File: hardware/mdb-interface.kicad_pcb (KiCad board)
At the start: 2 copper layers, 99.6 x 99.1 mm, 80 parts, among them IC1 ATMEGA644PA-A, J1 USB, K1 *, K2 *, P1 CONN_24, P10 CONN_1, P11 CONN_1, P12 CONN_1, P2 CONN_12V, P3 CONN_6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

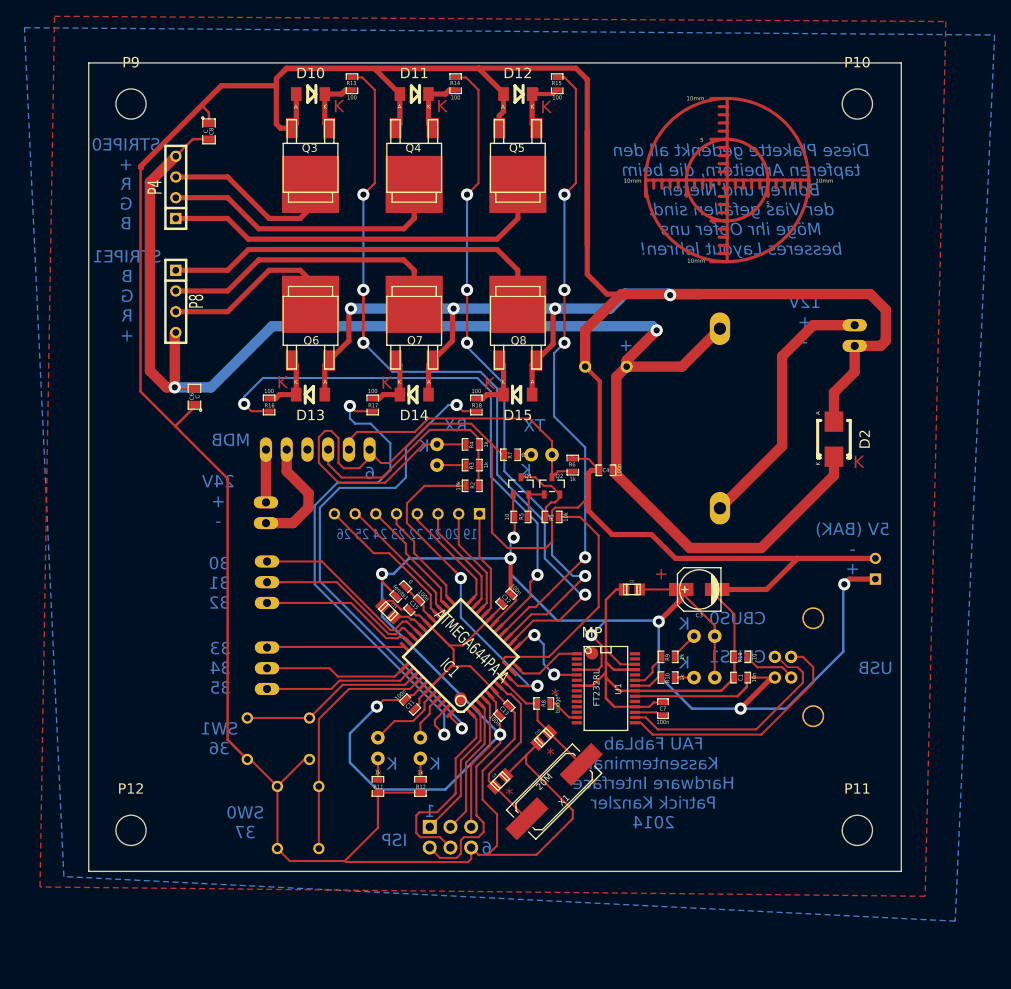
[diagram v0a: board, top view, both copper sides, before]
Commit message: Leiterplattenbemaßung gesäubert, fixes #14
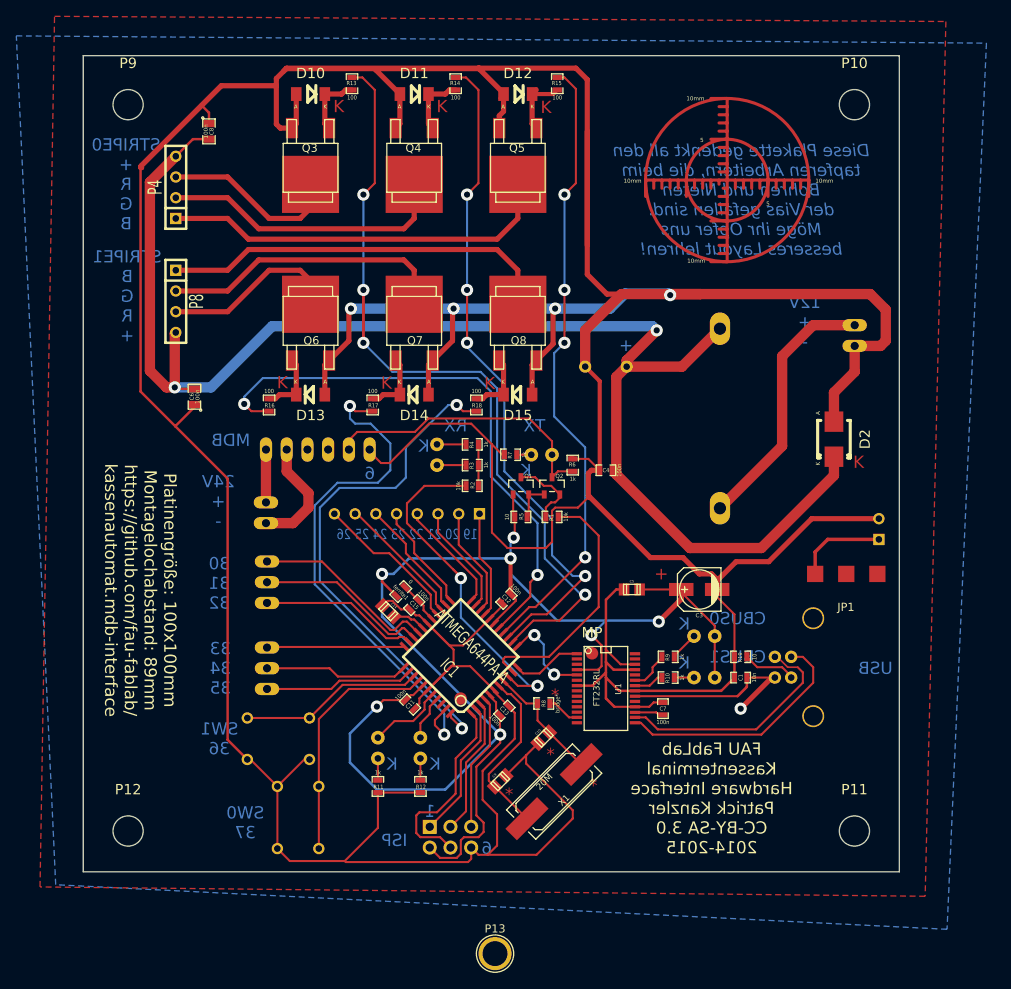
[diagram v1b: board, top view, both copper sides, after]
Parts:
- added JP1: JUMPER3, Oddities:NetTie-II_SMD, F.Cu at (163.4, 99.4)
- added P13: CONN_01X01, Connect:1pin, F.Cu at (120.4, 146.0)
- C6, C8: value C -> 100n
- moved P6 4.88 mm to (167.4, 93.9)
- moved P10 0.37 mm to (164.4, 41.9)
- moved P11 0.37 mm to (164.4, 130.9)
- moved P9 0.37 mm to (75.4, 41.9)
- moved P12 0.37 mm to (75.4, 130.9)
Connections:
- C1 pad 1: +5V -> /VUSB
- D1 pad 1: Net-(D1-Pad1) -> +5V
- D1 pad 2: GND -> Net-(D1-Pad2)
- J1 pad 1: +5V -> /VUSB
- P6 pad 1: +5V -> /VBAK
- R3 pad 1: /MDB_MR -> Net-(D1-Pad2)
- R3 pad 2: Net-(D1-Pad1) -> /MDB_MR
- R4 pad 1: /MDB_MR -> +5V
- R4 pad 2: GND -> /MDB_MR
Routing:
- net +5V: track 266.9 -> 206.2 mm, vias 9 -> 7
- net GND: track 875.1 -> 824.0 mm
- net /MDB_MR: track 30.4 -> 0.89 mm
- net /VUSB: track 0.00 -> 17.4 mm, vias 0 -> 1
- net /VBAK: track 0.00 -> 11.1 mm
- net Net-(D1-Pad2): track 0.00 -> 6.10 mm
- net Net-(D1-Pad1): track 3.56 -> 0.00 mm
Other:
- board size 99.6 x 99.1 mm -> 100 x 100 mm
- board text added: "FAU FabLab Kassenterminal Hardware Interface Patrick Kanzler CC-BY-SA 3.0 2014-2015"
- board text added: "Platinengröße: 100x100mm Montagelochabstand: 89mm https://github.com/fau-fablab/ kassenautomat.mdb-interface"
- board text removed: "FAU FabLab Kassenterminal Hardware Interface Patrick Kanzler 2014"

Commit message: Platine angepasst, bereit zur Fertigungsvorbereitung, fixes #11
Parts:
- removed MP (x2): Measurement_Point_Round-SMD-Pad_Small, Measurement_Points:Measurement_Point_Round-SMD-Pad_Small
- P13: footprint Connect:1pin -> Measurement_Points:Measurement_Point_Square-TH_Small
- moved P13 75.9 mm to (167.4, 86.4)
- moved Q2 1.17 mm to (128.5, 88.9), turned to 270 degrees
- moved Q1 1.02 mm to (124.1, 89.5), turned to 270 degrees
- turned D1 to 270 degrees
- turned R3 to 0 degrees
- turned R4 to 0 degrees
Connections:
- Q1 pad 1: +5V -> Net-(Q1-Pad1)
- Q1 pad 2: Net-(Q1-Pad2) -> +5V
- Q2 pad 1: Net-(Q1-Pad2) -> Net-(Q1-Pad3)
- Q2 pad 2: Net-(Q1-Pad3) -> Net-(Q1-Pad1)
- R5 pad 2: Net-(Q1-Pad2) -> Net-(Q1-Pad1)
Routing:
- net +5V: track 206.2 -> 277.8 mm, vias 7 -> 10
- net /MDB_MR: track 0.89 -> 28.3 mm
- net /VUSB: track 17.4 -> 41.9 mm, vias 1 -> 2
- net GND: track 824.0 -> 835.6 mm
- net Net-(Q1-Pad1): track 0.00 -> 9.72 mm
- net Net-(Q1-Pad2): track 4.74 -> 0.00 mm
- net Net-(D1-Pad2): track 6.10 -> 3.56 mm
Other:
- board text removed: "K"
- board text removed: "USB"

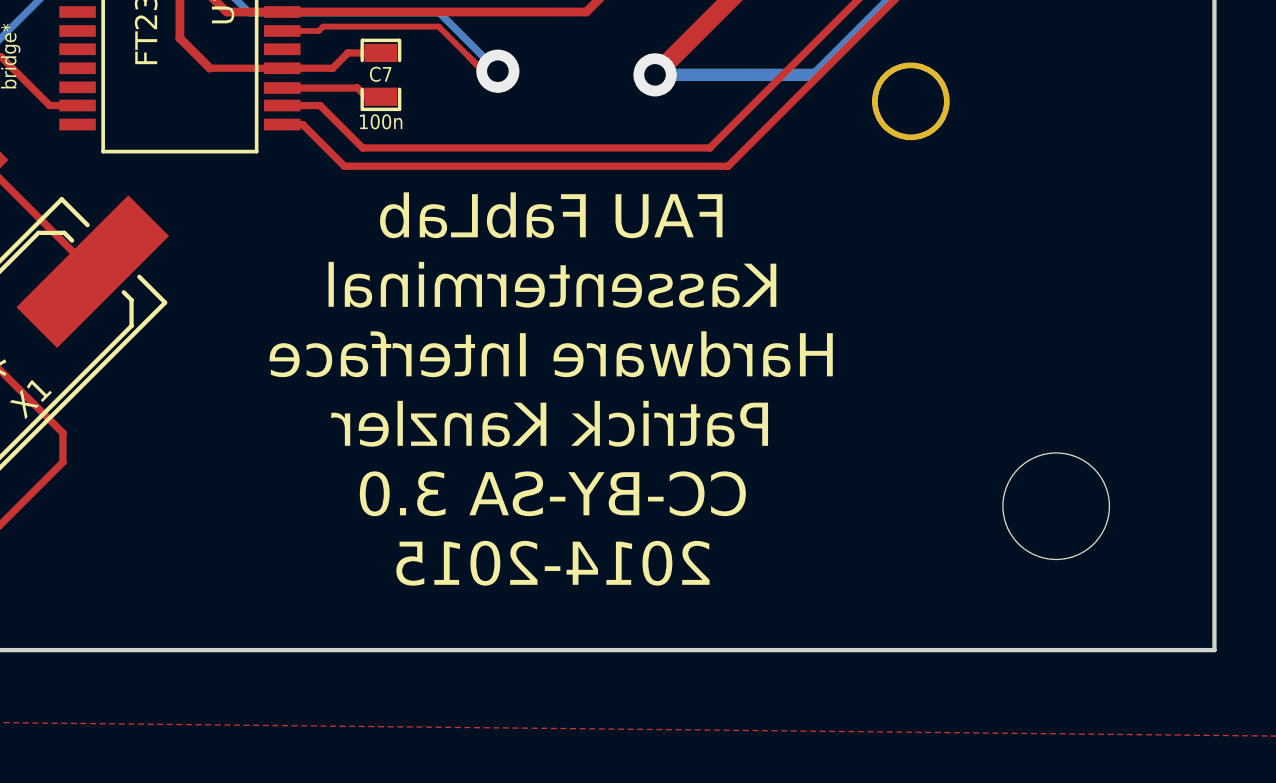
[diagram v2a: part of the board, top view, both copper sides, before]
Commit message: Platine aktualisiert: DRC stimmt jetzt für multi-cb und hat TOP/BOTTOM-Markierung
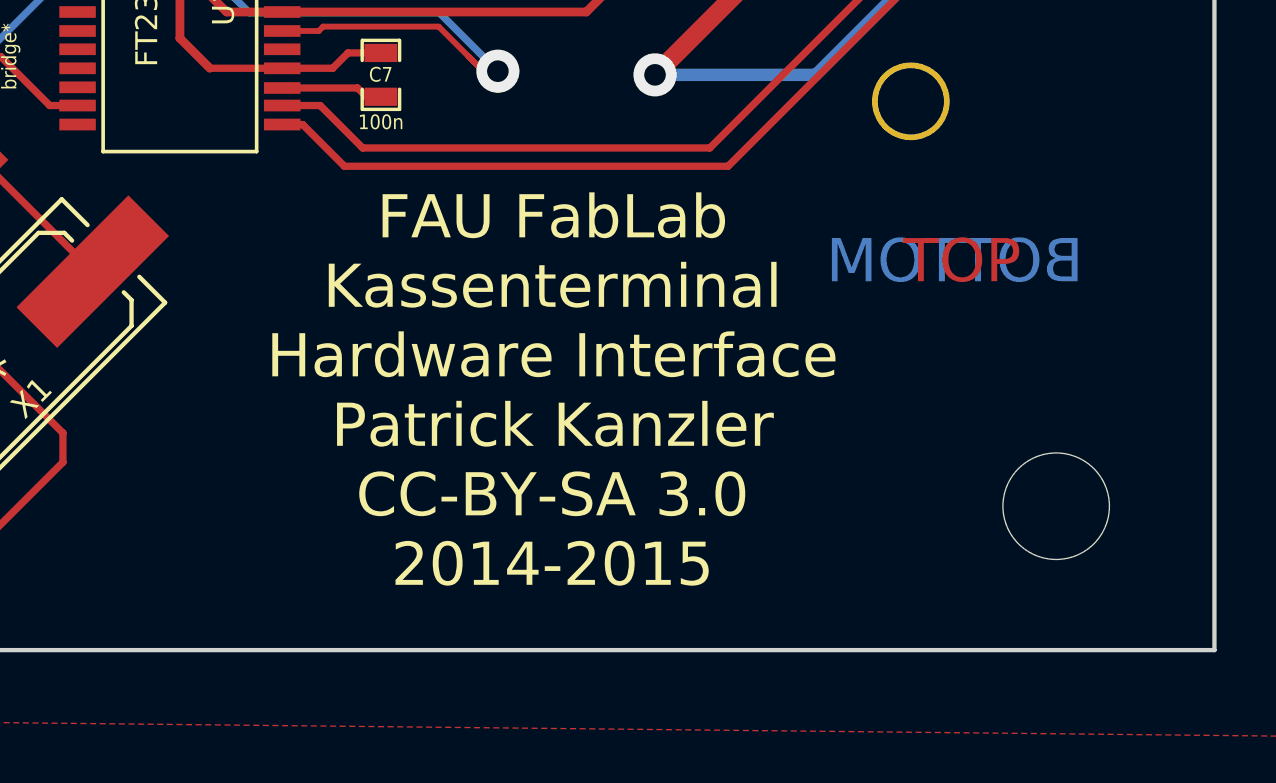
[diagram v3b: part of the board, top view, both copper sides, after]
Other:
- net class Default: clearance 0.254 -> 0.075
- rule trace_clearance: 0.254 -> 0.075
- board text added: "BOTTOM"
- board text added: "TOP"
